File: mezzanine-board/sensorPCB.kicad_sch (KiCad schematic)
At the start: 20 parts, among them U3 AS72652, U4 AS72653, U6 AS72651

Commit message: Add Molex 90122-0140 right-angle header to main board libraries
Import the Library Loader (SamacSys) part into the main board: footprint
into the registered SamacSys_Parts.pretty, 3D model into
SamacSys_Parts.3dshapes, and symbol appended to SamacSys_Parts.kicad_sym
(3D path rewritten to ${KIPRJMOD}-relative, Footprint property qualified
with the library nickname).

Register SamacSys_Parts as a symbol library in the main board's
sym-lib-table (previously only its footprints were registered).
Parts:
- added J1: 90152-2140, SamacSys_Parts:901522140, symbol SamacSys_Parts:90152-2140
- U3, U4: footprint SparkfunLibrary:AS72651 -> SamacSys_Parts:AS72651BLGT
- U6: footprint Package_LGA:AMS_LGA-20_4.7x4.5mm_P0.65mm -> SamacSys_Parts:AS72651BLGT

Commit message: Add TE 215307-7 connector to mezzanine libraries
Import the Library Loader part (14-pin TE Connectivity connector) into
the mezzanine's already-registered SamacSys_Parts library: footprint, 3D
model, and symbol appended. 3D path rewritten to ${KIPRJMOD}-relative and
the symbol's Footprint property qualified with the library nickname.
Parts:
- removed J1: 90152-2140, SamacSys_Parts:901522140, symbol SamacSys_Parts:90152-2140
- added J2: SSQ-120-04-G-D, SamacSys_Parts:SSQ-120-XX-YYY-D, symbol SamacSys_Parts:SSQ-120-04-G-D

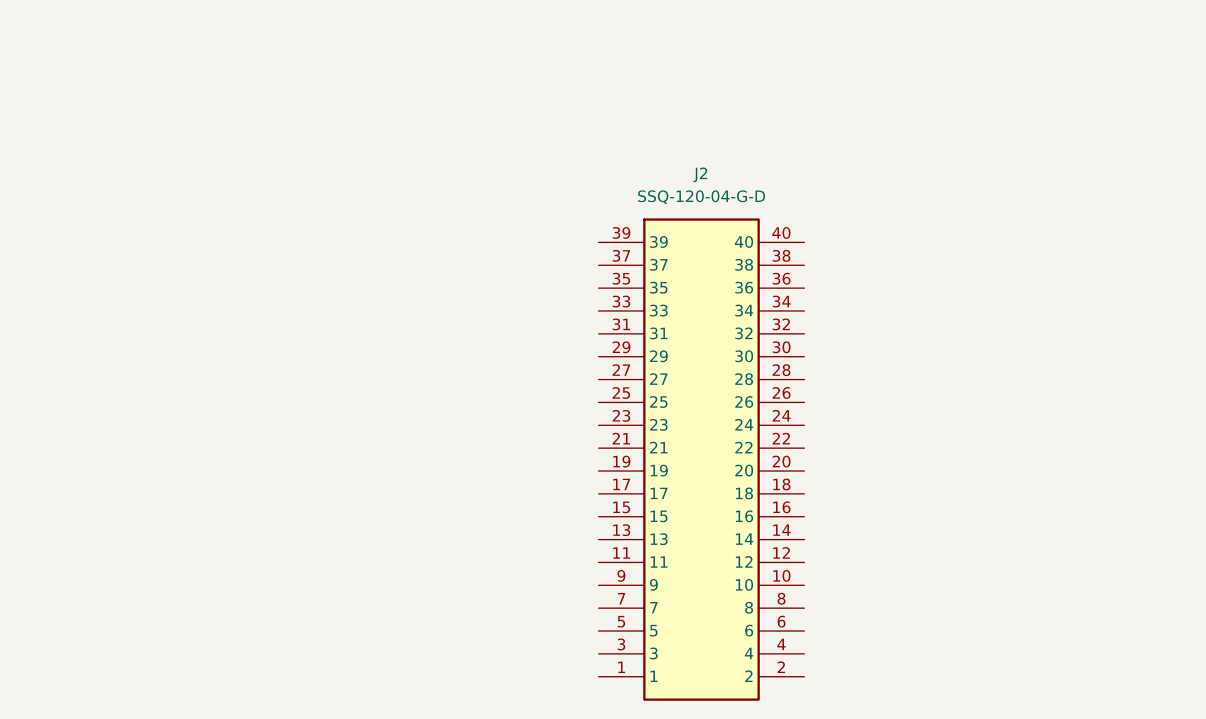
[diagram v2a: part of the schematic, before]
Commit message: Add Samtec FTSH-110-01-F-D-RA header to mezzanine libraries
Import the Library Loader part (2x10 right-angle 1.27mm fine-pitch header)
into the mezzanine's SamacSys_Parts library: footprint, 3D model, and
symbol appended. 3D path rewritten to ${KIPRJMOD}-relative and the
symbol's Footprint property qualified with the library nickname.
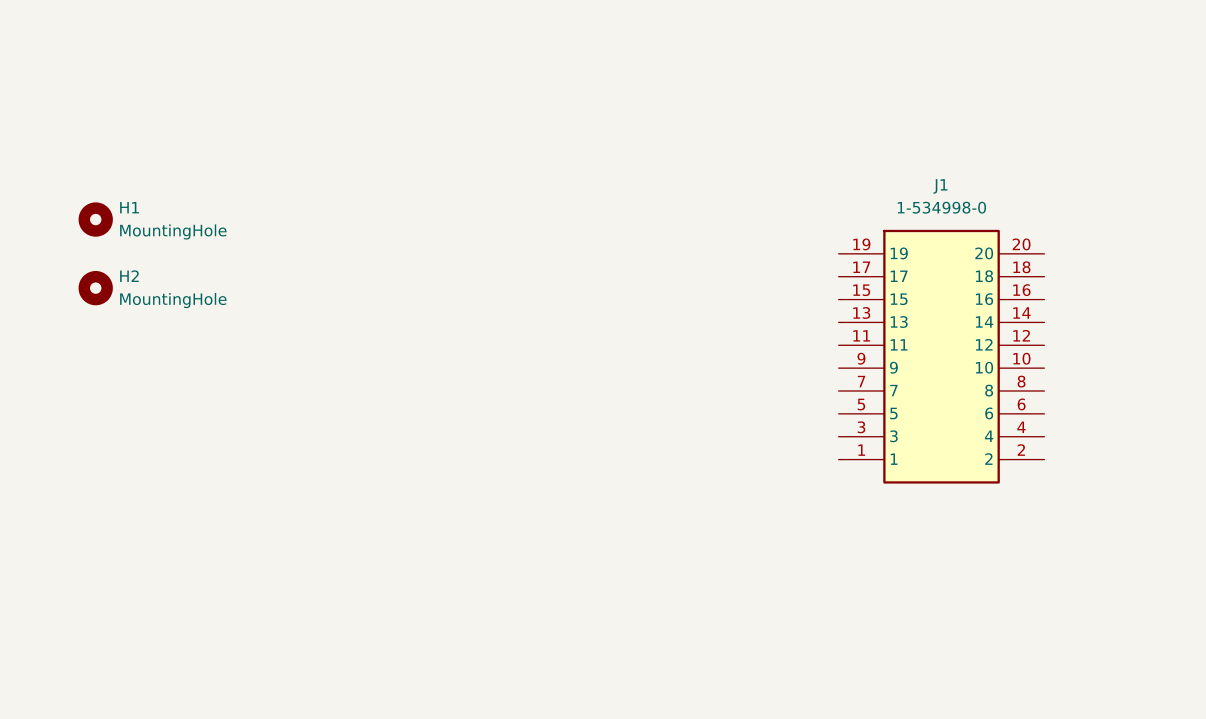
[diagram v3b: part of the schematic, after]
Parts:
- removed J2: SSQ-120-04-G-D, SamacSys_Parts:SSQ-120-XX-YYY-D, symbol SamacSys_Parts:SSQ-120-04-G-D
- added H1, H2: MountingHole, symbol Mechanical:MountingHole
- added J1: 1-534998-0, SamacSys_Parts:15349980, symbol SamacSys_Parts:1-534998-0

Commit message: Add Amphenol 20021311-00020T4LF (Minitek127) to mezzanine libraries
Import the Library Loader part (20-pin 1.27mm board-to-board connector)
into the mezzanine's SamacSys_Parts library: footprint, 3D model, and
symbol appended. 3D path rewritten to ${KIPRJMOD}-relative and the
symbol's Footprint property qualified with the library nickname.
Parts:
- H1, H2: footprint (none) -> Mounting_Wuerth:Mounting_Wuerth_WA-SMSI-M2.5_H0.5mm_9774005151
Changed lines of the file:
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@@
 			)
 		)
-		(property "Footprint" ""
+		(property "Footprint" "Mounting_Wuerth:Mounting_Wuerth_WA-SMSI-M2.5_H0.5mm_9774005151"
 			(at 25.4 101.6 0)
 			(hide yes)
@@
 			)
 		)
-		(property "Footprint" ""
+		(property "Footprint" "Mounting_Wuerth:Mounting_Wuerth_WA-SMSI-M2.5_H0.5mm_9774005151"
 			(at 25.4 109.22 0)
 			(hide yes)

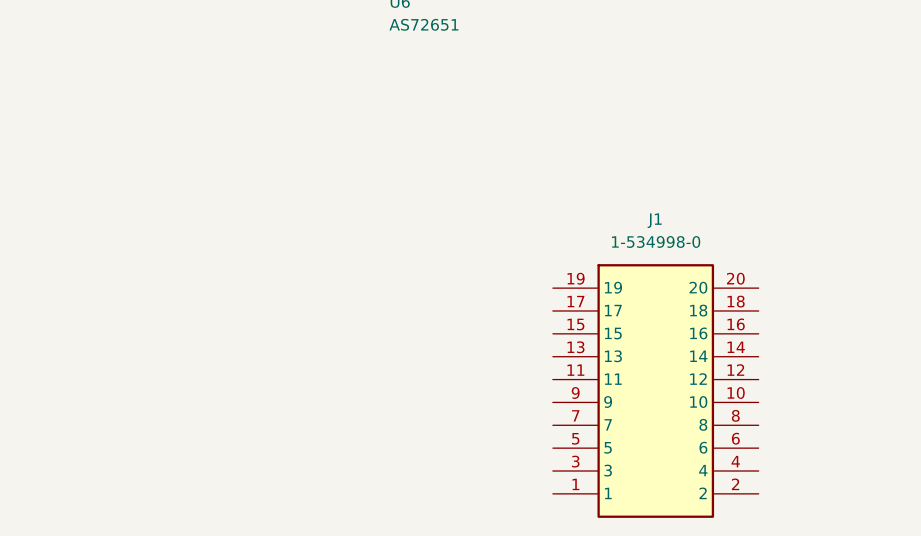
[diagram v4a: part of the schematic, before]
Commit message: Add Samtec FTSH-105-04-L-D-RA and SFMC-105-01-L-D to both boards
Import two Library Loader parts (a 2x5 1.27mm right-angle header and its
mating 2x5 socket strip) into the SamacSys_Parts library of BOTH the main
board and the mezzanine board: footprints, 3D models, and symbols
appended. 3D paths rewritten to ${KIPRJMOD}-relative and each symbol's
Footprint property qualified with the library nickname.
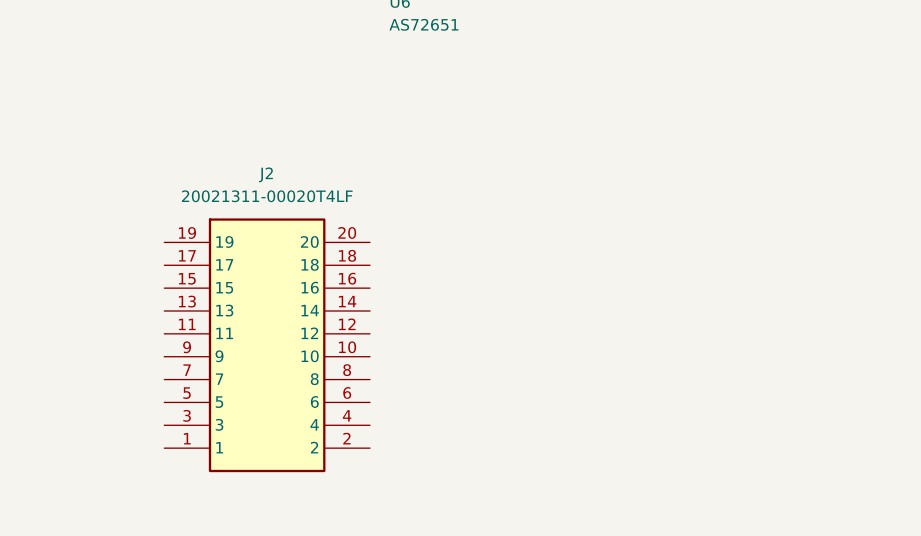
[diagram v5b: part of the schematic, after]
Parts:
- removed J1: 1-534998-0, SamacSys_Parts:15349980, symbol SamacSys_Parts:1-534998-0
- added J2: 20021311-00020T4LF, SamacSys_Parts:2002131100020T4LF, symbol SamacSys_Parts:20021311-00020T4LF
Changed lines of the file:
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@@
-	)
-	(symbol
-		(lib_id "SamacSys_Parts:1-534998-0")
-		(at 107.95 105.41 0)
-		(unit 1)
-		(body_style 1)
-		(exclude_from_sim no)
-		(in_bom yes)
-		(on_board yes)
-		(in_pos_files yes)
-		(dnp no)
-		(fields_autoplaced yes)
-		(property "Reference" "J1"
-			(at 119.38 97.79 0)
-			(show_name no)
-			(do_not_autoplace no)
-			(effects
-				(font
-					(size 1.27 1.27)
-				)
-			)
-		)
-		(property "Value" "1-534998-0"
-			(at 119.38 100.33 0)
-			(show_name no)
-			(do_not_autoplace no)
-			(effects
-				(font
-					(size 1.27 1.27)
-				)
-			)
-		)
-		(property "Footprint" "SamacSys_Parts:15349980"
-			(at 127 200.33 0)
-			(hide yes)
-			(show_name no)
-			(do_not_autoplace no)
-			(effects
-				(font
-					(size 1.27 1.27)
-				)
-				(justify left top)
-			)
-		)
-		(property "Datasheet" "https://www.te.com/commerce/DocumentDelivery/DDEController?Action=srchrtrv&DocNm=534998&DocType=Customer%20Drawing&DocLang=English&DocFormat=pdf&PartCntxt=1-534998-0"
-			(at 127 300.33 0)
-			(hide yes)
-			(show_name no)
-			(do_not_autoplace no)
-			(effects
-				(font
-					(size 1.27 1.27)
-				)
-				(justify left top)
-			)
-		)
-		(property "Description" "TE Connectivity Mod IV Series 20 Way 2 Row Female Straight PCB Connector Housing"
-			(at 107.95 105.41 0)
-			(hide yes)
-			(show_name no)
-			(do_not_autoplace no)
-			(effects
-				(font
-					(size 1.27 1.27)
-				)
-			)
-		)
-		(property "Height" "6.86"
-			(at 127 500.33 0)
-			(hide yes)
-			(show_name no)
-			(do_not_autoplace no)
-			(effects
-				(font
-					(size 1.27 1.27)
-				)
-				(justify left top)
-			)
-		)
-		(property "Manufacturer_Name" "TE Connectivity"
-			(at 127 600.33 0)
-			(hide yes)
-			(show_name no)
-			(do_not_autoplace no)
-			(effects
-				(font
-					(size 1.27 1.27)
-				)
-				(justify left top)
-			)
-		)
-		(property "Manufacturer_Part_Number" "1-534998-0"
-			(at 127 700.33 0)
-			(hide yes)
-			(show_name no)
-			(do_not_autoplace no)
-			(effects
-				(font
-					(size 1.27 1.27)
-				)
-				(justify left top)
-			)
-		)
-		(property "Mouser Part Number" "571-1534998"
-			(at 127 800.33 0)
-			(hide yes)
-			(show_name no)
-			(do_not_autoplace no)
-			(effects
-				(font
-					(size 1.27 1.27)
-				)
-				(justify left top)
-			)
-		)
-		(property "Mouser Price/Stock" "https://www.mouser.co.uk/ProductDetail/TE-Connectivity/1-534998-0?qs=HSGlLeu24BNCQWOVWjHQgA%3D%3D"
-			(at 127 900.33 0)
-			(hide yes)
-			(show_name no)
-			(do_not_autoplace no)
-			(effects
-				(font
-					(size 1.27 1.27)
-				)
-				(justify left top)
-			)
-		)
-		(property "Arrow Part Number" "1-534998-0"
-			(at 127 1000.33 0)
-			(hide yes)
-			(show_name no)
-			(do_not_autoplace no)
-			(effects
-				(font
-					(size 1.27 1.27)
-				)
-				(justify left top)
-			)
-		)
-		(property "Arrow Price/Stock" "https://www.arrow.com/en/products/1-534998-0/te-connectivity?region=nac"
-			(at 127 1100.33 0)
-			(hide yes)
-			(show_name no)
-			(do_not_autoplace no)
-			(effects
-				(font
-					(size 1.27 1.27)
-				)
-				(justify left top)
-			)
-		)
-		(pin "4"
-		)
-		(pin "17"
-		)
-		(pin "11"
-		)
-		(pin "9"
-		)
-		(pin "14"
-		)
-		(pin "7"
-		)
-		(pin "6"
-		)
-		(pin "10"
-		)
-		(pin "12"
-		)
-		(pin "2"
-		)
-		(pin "5"
-		)
-		(pin "8"
-		)
-		(pin "15"
-		)
-		(pin "1"
-		)
-		(pin "13"
-		)
-		(pin "16"
-		)
-		(pin "19"
-		)
-		(pin "3"
-		)
-		(pin "18"
-		)
-		(pin "20"
-		)
-		(instances
-			(project "sensorPCB"
-				(path "/1c4f14d6-6222-4843-aaf4-88e85cc8a419"
-					(reference "J1")
-					(unit 1)
-				)
-			)
-		)
 	)
 	(symbol
@@
 					(unit 1)
 				)
+			)
+		)
+	)
+	(symbol
+		(lib_id "SamacSys_Parts:20021311-00020T4LF")
+		(at 64.77 100.33 0)
+		(unit 1)
+		(body_style 1)
+		(exclude_from_sim no)
+		(in_bom yes)
+		(on_board yes)
+		(in_pos_files yes)
+		(dnp no)
+		(fields_autoplaced yes)
+		(property "Reference" "J2"
+			(at 76.2 92.71 0)
+			(show_name no)
+			(do_not_autoplace no)
+			(effects
+				(font
+					(size 1.27 1.27)
+				)
+			)
+		)
+		(property "Value" "20021311-00020T4LF"
+			(at 76.2 95.25 0)
+			(show_name no)
+			(do_not_autoplace no)
+			(effects
+				(font
+					(size 1.27 1.27)
+				)
+			)
+		)
+		(property "Footprint" "SamacSys_Parts:2002131100020T4LF"
+			(at 83.82 195.25 0)
+			(hide yes)
+			(show_name no)
+			(do_not_autoplace no)
+			(effects
+				(font
+					(size 1.27 1.27)
+				)
+				(justify left top)
+			)
+		)
+		(property "Datasheet" "https://cdn.amphenol-cs.com/media/wysiwyg/files/drawing/20021311.pdf"
+			(at 83.82 295.25 0)
+			(hide yes)
+			(show_name no)
+			(do_not_autoplace no)
+			(effects
+				(font
+					(size 1.27 1.27)
+				)
+				(justify left top)
+			)
+		)
+		(property "Description" "20 Position Receptacle Connector 0.050\" (1.27mm) Through Hole Gold -55C ~ 125C Board to Board"
+			(at 64.77 100.33 0)
+			(hide yes)
+			(show_name no)
+			(do_not_autoplace no)
+			(effects
+				(font
+					(size 1.27 1.27)
+				)
+			)
+		)
+		(property "Height" "4.6"
+			(at 83.82 495.25 0)
+			(hide yes)
+			(show_name no)
+			(do_not_autoplace no)
+			(effects
+				(font
+					(size 1.27 1.27)
+				)
+				(justify left top)
+			)
+		)
+		(property "Manufacturer_Name" "Amphenol"
+			(at 83.82 595.25 0)
+			(hide yes)
+			(show_name no)
+			(do_not_autoplace no)
+			(effects
+				(font
+					(size 1.27 1.27)
+				)
+				(justify left top)
+			)
+		)
+		(property "Manufacturer_Part_Number" "20021311-00020T4LF"
+			(at 83.82 695.25 0)
+			(hide yes)
+			(show_name no)
+			(do_not_autoplace no)
+			(effects
+				(font
+					(size 1.27 1.27)
+				)
+				(justify left top)
+			)
+		)
+		(property "Mouser Part Number" "649-221311-00020T4LF"
+			(at 83.82 795.25 0)
+			(hide yes)
+			(show_name no)
+			(do_not_autoplace no)
+			(effects
+				(font
+					(size 1.27 1.27)
+				)
+				(justify left top)
+			)
+		)
+		(property "Mouser Price/Stock" "https://www.mouser.co.uk/ProductDetail/Amphenol-FCI/20021311-00020T4LF?qs=oJs1R%252BxK6kS%2FgHfbOlCkOg%3D%3D"
+			(at 83.82 895.25 0)
+			(hide yes)
+			(show_name no)
+			(do_not_autoplace no)
+			(effects
+				(font
+					(size 1.27 1.27)
+				)
+				(justify left top)
+			)
+		)
+		(property "Arrow Part Number" ""
+			(at 83.82 995.25 0)
+			(hide yes)
+			(show_name no)
+			(do_not_autoplace no)
+			(effects
+				(font
+					(size 1.27 1.27)
+				)
+				(justify left top)
+			)
+		)
+		(property "Arrow Price/Stock" ""
+			(at 83.82 1095.25 0)
+			(hide yes)
+			(show_name no)
+			(do_not_autoplace no)
+			(effects
+				(font
+					(size 1.27 1.27)
+				)
+				(justify left top)
+			)
+		)
+		(pin "20"
+		)
+		(pin "15"
+		)
+		(pin "12"
+		)
+		(pin "16"
+		)
+		(pin "17"
+		)
+		(pin "19"
+		)
+		(pin "13"
+		)
+		(pin "14"
+		)
+		(pin "18"
+		)
+		(pin "3"
+		)
+		(pin "7"
+		)
+		(pin "4"
+		)
+		(pin "6"
+		)
+		(pin "5"
+		)
+		(pin "1"
+		)
+		(pin "8"
+		)
+		(pin "10"
+		)
+		(pin "9"
+		)
+		(pin "11"
+		)
+		(pin "2"
+		)
+		(instances
+			(project "sensorPCB"
+				(path "/1c4f14d6-6222-4843-aaf4-88e85cc8a419"
+					(reference "J2")
+					(unit 1)
+				)

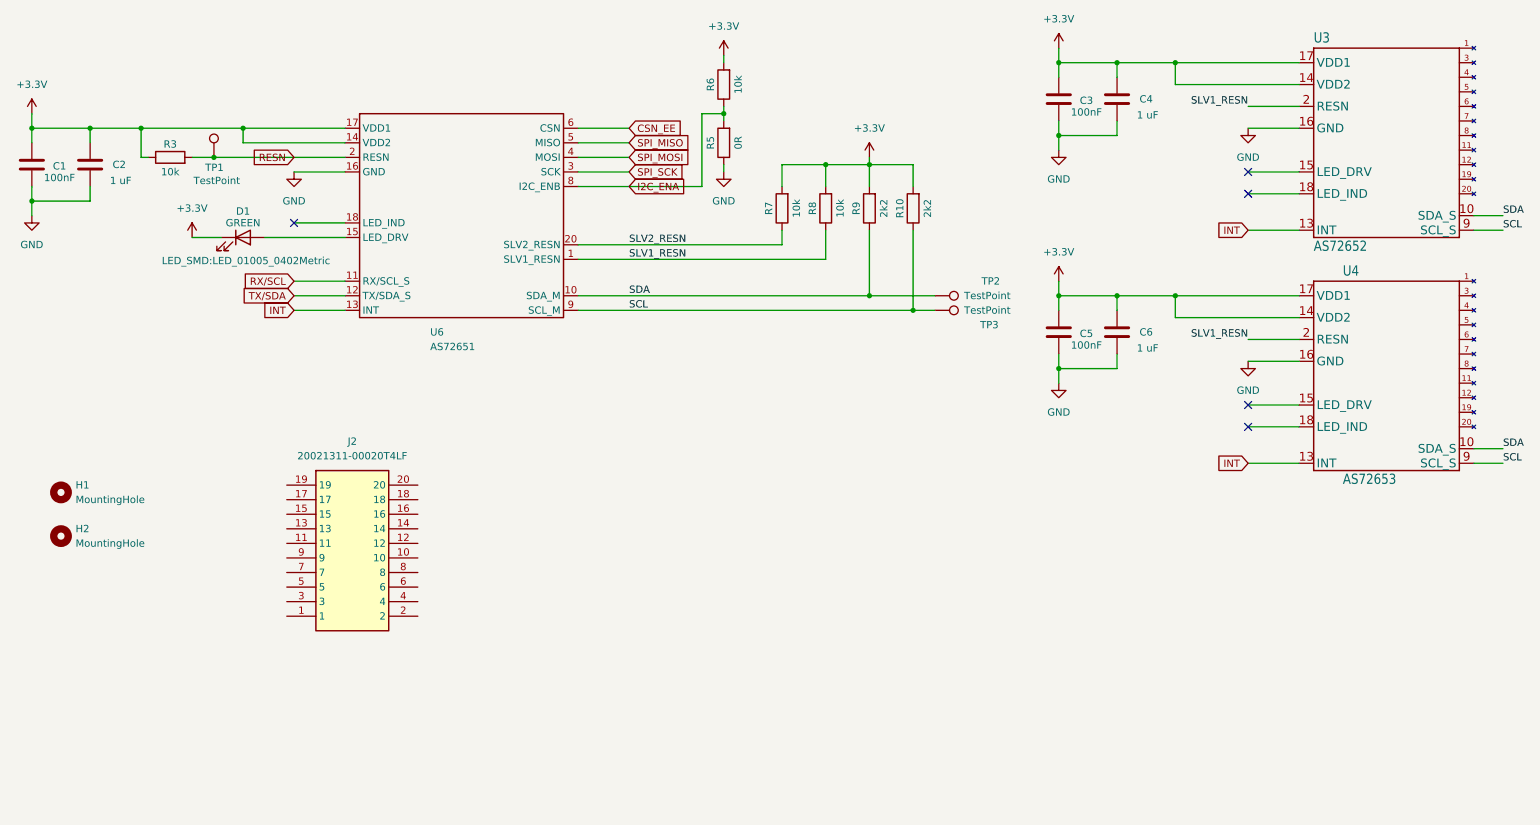
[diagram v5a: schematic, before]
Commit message: Attach Raspberry Pi Zero 2 W 3D model to RPi footprint
Add the mechanical STEP model of the Raspberry Pi Zero 2 W board
(RaspberryPi_Zero_2W.step, from the downloaded SolidWorks CAD) to
main-board 3dmodels, and reference it from the RASPBERRYPI-ZERO_RPI-ZERO
footprint via a ${KIPRJMOD}-relative path. Offset/rotation set to zero as
a starting point - needs alignment tuning in KiCad's 3D tab.
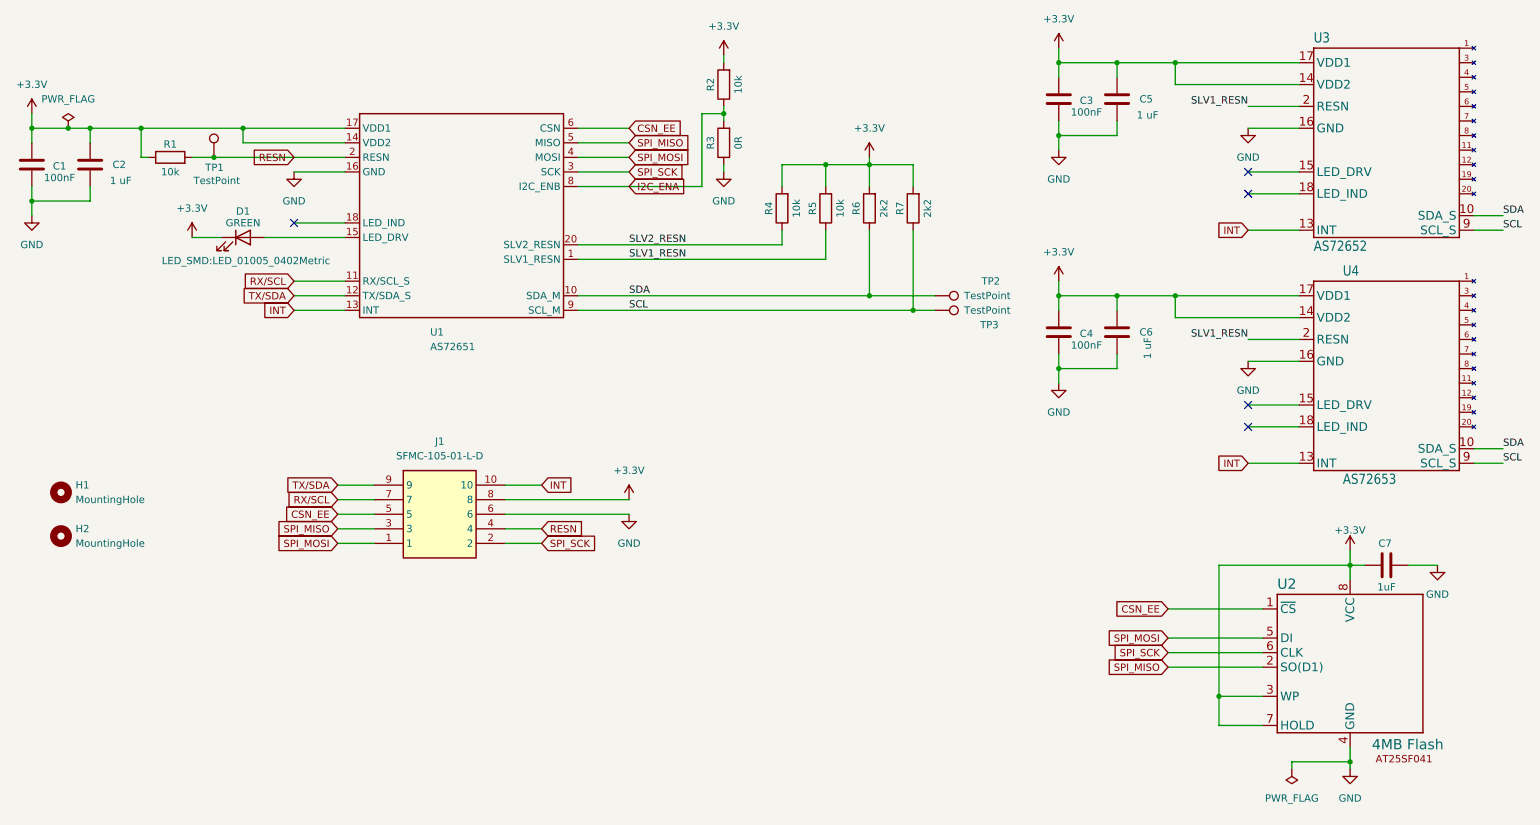
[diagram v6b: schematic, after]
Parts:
- removed J2: 20021311-00020T4LF, SamacSys_Parts:2002131100020T4LF, symbol SamacSys_Parts:20021311-00020T4LF
- added C7: 1uF, SparkfunLibrary:0603, symbol Device:C
- added J1: SFMC-105-01-L-D, SamacSys_Parts:SFMC-105-XX-YY-D, symbol SamacSys_Parts:SFMC-105-01-L-D
- added U2: 4MB Flash, SparkfunLibrary:4MbFlash, symbol Qwiic_Spectral_Sensor-AS7265x-eagle-import:AT25SF041
- renumbered C5 to C4, C4 to C5, R3 to R1, R6 to R2, R5 to R3, R7 to R4, R8 to R5, R9 to R6, R10 to R7, U6 to U1
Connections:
- net +3.3V: now also C7.1, J1.8, U2.3 (WP), U2.7 (HOLD), U2.8 (VCC)
- net CSN_EE: now also J1.5, U2.1 (~{CS})
- net GND: now also C7.2, J1.6, U2.4 (GND)
- net INT: now also J1.10
- net RESN: now also J1.4
- net RX/SCL: now also J1.7
- net SPI_MISO: now also J1.3, U2.2 (SO(D1))
- net SPI_MOSI: now also J1.1, U2.5 (DI)
- net SPI_SCK: now also J1.2, U2.6 (CLK)
- net TX/SDA: now also J1.9

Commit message: Initial sensor board routing
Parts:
- removed TP1, TP2, TP3: TestPoint, TestPoint:TestPoint_Pad_D1.0mm, symbol Connector:TestPoint

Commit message: Fixed warnings
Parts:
- D1: footprint LED_SMD:LED_01005_0402Metric -> LED_SMD:LED_0603_1608Metric
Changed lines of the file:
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@@
 			)
 		)
-		(property "Footprint" "LED_SMD:LED_01005_0402Metric"
+		(property "Footprint" "LED_SMD:LED_0603_1608Metric"
 			(at 57.658 61.214 0)
 			(show_name no)
